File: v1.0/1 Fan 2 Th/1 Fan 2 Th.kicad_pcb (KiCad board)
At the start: 2 copper layers, 80 x 75 mm, 48 parts, among them J1 POWER_HARNESS, J2 UPDI, J3 TH1, J4 FAN1, J5 LED_PANEL, J7 TH2, J8 BUZZER_HARNESS, Q1 DMPH4029LFGQ, Q2 AO3400A, Q4 AO3400A, U1 CJ7533S, U2 ATTINY1616-SNR

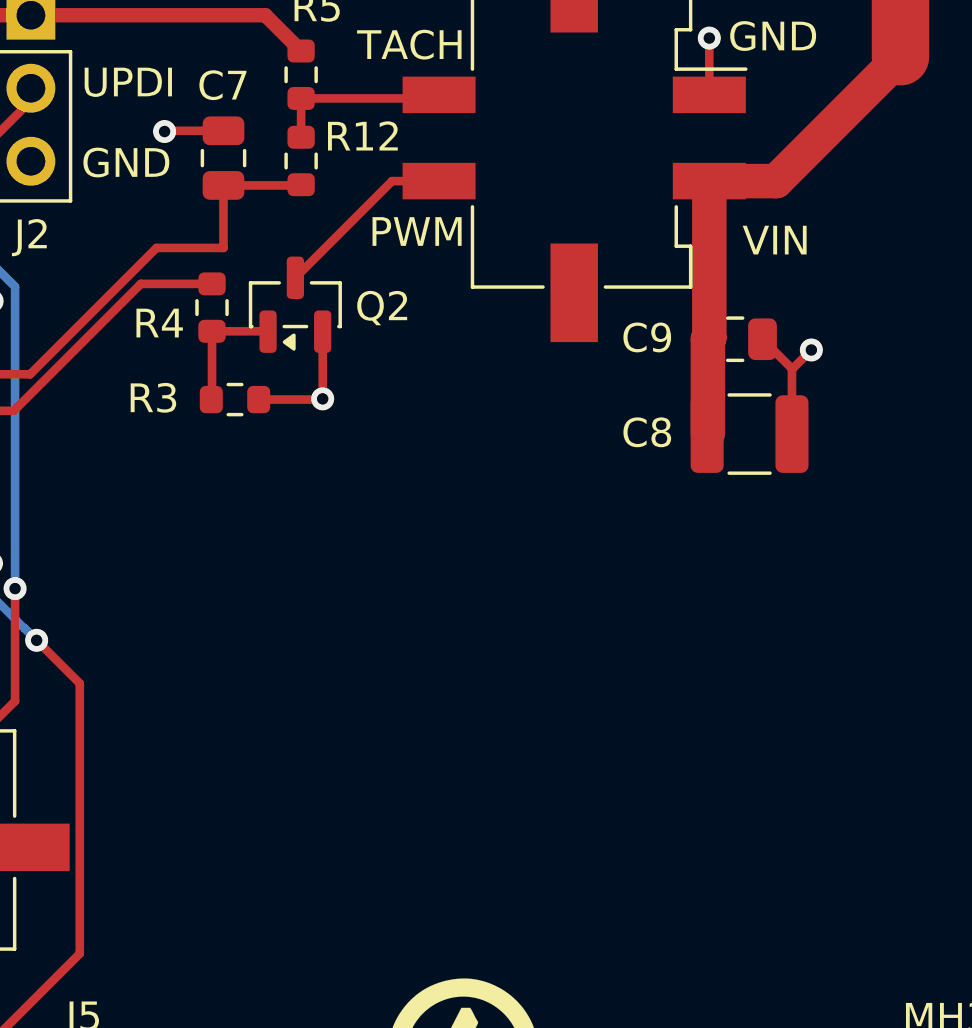
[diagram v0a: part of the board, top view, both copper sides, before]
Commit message: added 5v rail
added 5v rail for pwm concerns of the fans
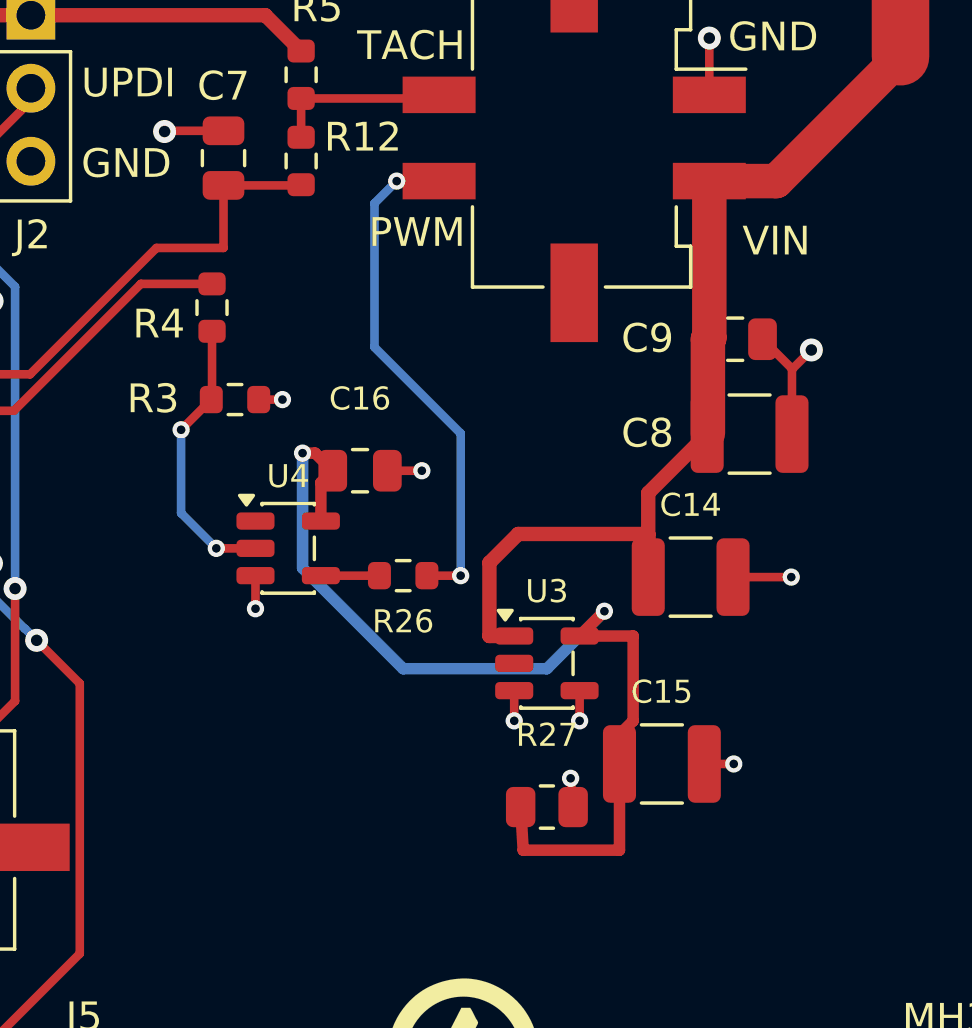
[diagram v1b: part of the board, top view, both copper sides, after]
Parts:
- removed Q2: AO3400A, Package_TO_SOT_SMD:SOT-23
- added C14: 10 µF 50 V, Capacitor_SMD:C_1210_3225Metric, F.Cu at (99.0, 82.0)
- added C15: 10 µF 50 V, Capacitor_SMD:C_1210_3225Metric, F.Cu at (98.0, 88.5)
- added C16: 100 nF 50 V, Capacitor_SMD:C_0805_2012Metric, F.Cu at (87.5, 78.3)
- added R26: 33 Ω, Resistor_SMD:R_0603_1608Metric, F.Cu at (89.0, 82.0)
- added R27: 330 Ω, Resistor_SMD:R_0805_2012Metric, F.Cu at (94.0, 90.0)
- added U3: TPS7B6950QDBVRQ1, Package_TO_SOT_SMD:SOT-23-5, F.Cu at (94.0, 85.0)
- added U4: SN74AHCT1G04DBVR, Package_TO_SOT_SMD:SOT-23-5, F.Cu at (85.0, 81.0)
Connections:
- net Net-(Q2-G) renamed /FAN1_PWM_IN
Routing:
- net /+5V_PWM: track 0.00 -> 35.6 mm, vias 0 -> 2
- net /VIN_PROTECTED: track 141.0 -> 157.7 mm
- net /FAN1_PWM: track 6.39 -> 17.9 mm, vias 0 -> 2
- net /FAN1_PWM_IN: track 4.34 -> 9.87 mm, vias 0 -> 2
- net GND: track 51.5 -> 56.2 mm, vias 16 -> 23
- net /FAN1_PWM_DRIVE: track 0.00 -> 2.04 mm

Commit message: simulations & silkscreen edits
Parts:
- R10, R11, R14, R16, R17, R6, R8, R9: value 220 Ω -> 150 Ω
- moved U3 16.1 mm to (108.0, 77.0)
- moved R27 14.9 mm to (108.0, 85.0)
- moved C15 14.8 mm to (111.0, 81.5)
- moved C14 14.1 mm to (109.0, 72.0), turned to 180 degrees
- moved MH2 10.0 mm to (117.9, 38.5)
- moved MH3 10.0 mm to (117.9, 101.5)
- moved C16 1.70 mm to (87.5, 76.6)
- moved R26 1.70 mm to (89.0, 80.2)
- moved U4 1.70 mm to (85.0, 79.3)
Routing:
- net /VIN_PROTECTED: track 157.7 -> 195.9 mm
- net /+5V_PWM: track 35.6 -> 44.5 mm
- net /FAN1_PWM: track 17.9 -> 16.2 mm
- net /FAN1_PWM_IN: track 9.87 -> 8.53 mm
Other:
- board size 80 x 75 mm -> 90 x 75 mm
- board text added: "Designed in Cyprus"
- board text added: "NC"
